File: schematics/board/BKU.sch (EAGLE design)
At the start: 83 parts, among them IC1 MAX809REUR, IC2 MAX809REUR, J1 idc_2x5, J2 idc_2x5, Q1 8MHz, Q2 32,768KHz, SW1 RST, SW2 RST, U1 STM32F405RGT6

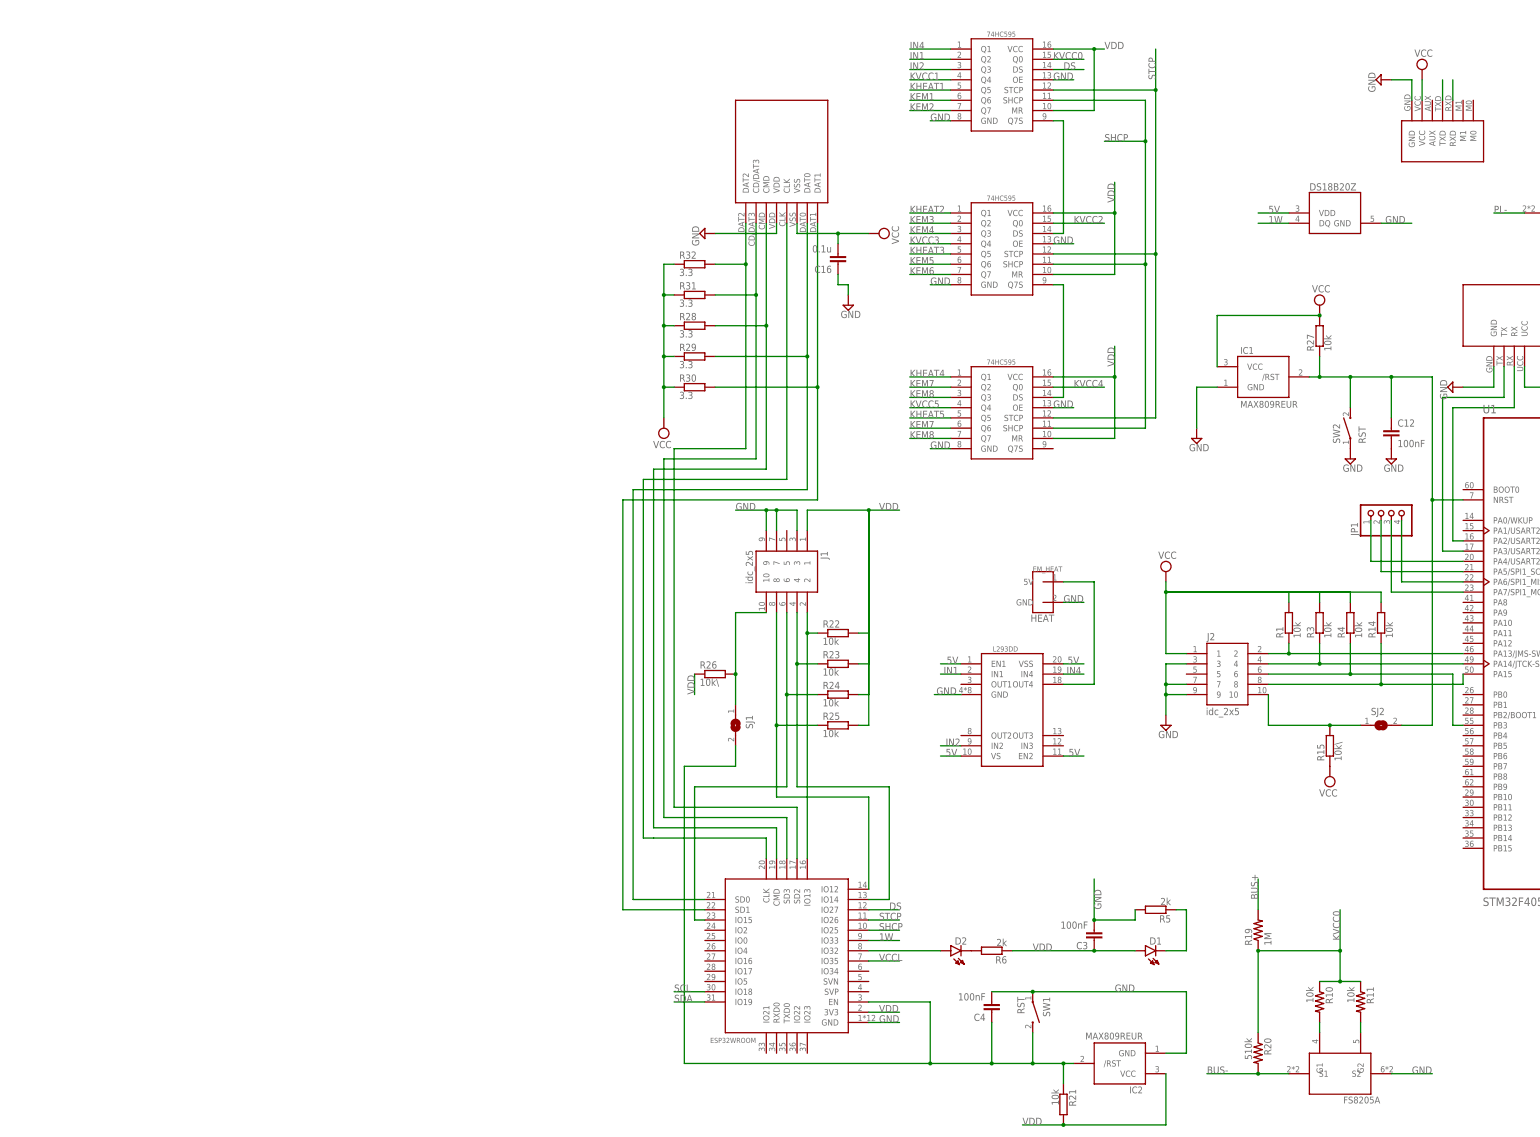
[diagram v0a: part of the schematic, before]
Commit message: доработана схема БСК1
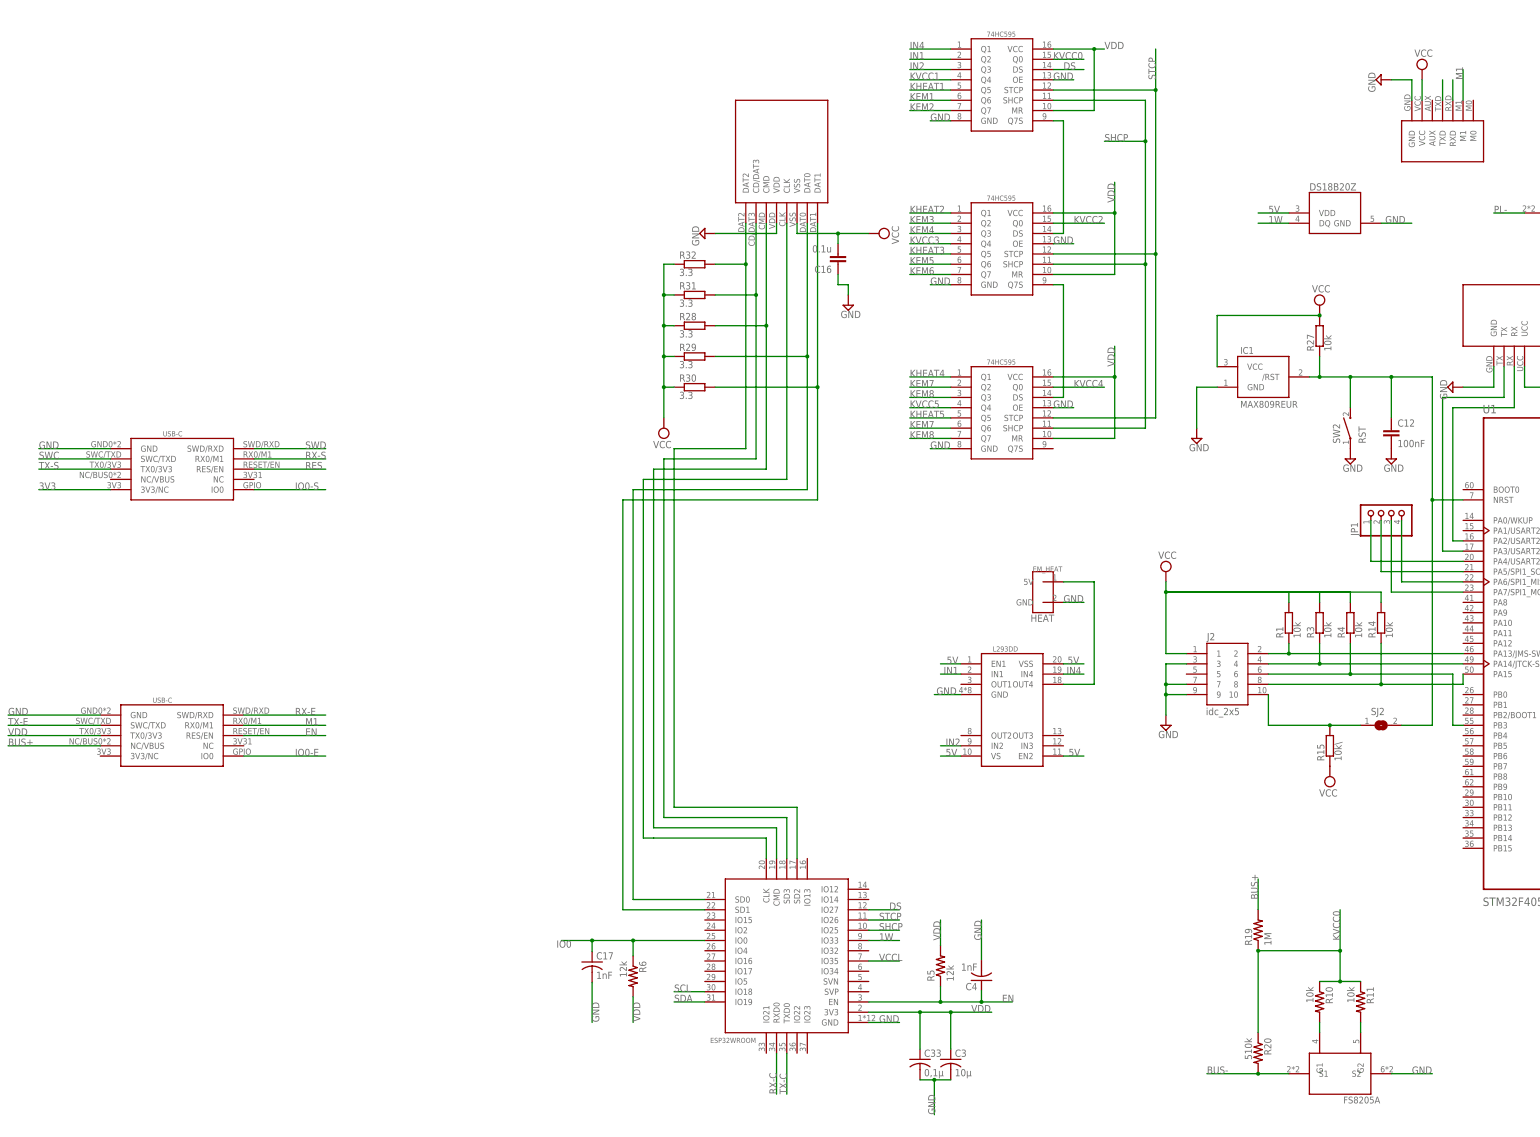
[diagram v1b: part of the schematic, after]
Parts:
- removed D1, D2: HLMP6, display-hp:HLMP6
- removed IC2: MAX809REUR, MAX809_:MAX809EUR
- removed J1: idc_2x5, idc_2x5:3221-10-0100-00
- removed R21, R22, R23, R24, R25: 10k, resistor-shunt:BVS
- removed R26: 10k\, resistor-shunt:BVS
- removed SJ1: (no value), jumper:SJW
- removed SW1: RST, 1437566-3:1437566-3
- added C17: 1nF, rcl:C-USC0603
- added C33: 0,1µ, rcl:C-USC0603
- added U$4, U$6: USB-C, CanCubeSat:USB-C
- C3: value 100nF -> 10µ; device rcl:C-EUC0603 -> rcl:C-USC0603
- C4: value 100nF -> 1nF; device rcl:C-EUC0603 -> rcl:C-USC0603
- R5, R6: value 2k -> 12k; device resistor-shunt:BVS -> resistor:R-US_R0603
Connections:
- removed net N$17: D1.K, R5.2
- removed net N$18: D2.K, R6.1
- removed net N$21: C4.1, IC2./RST, R21.2, SJ1.2, SW1.2, U$13.EN
- removed net N$22: J1.2, R22.2, U$13.IO13
- removed net N$23: J1.4, R23.2, U$13.IO14
- removed net N$26: J1.8, R25.2, U$13.IO12
- removed net N$27: J1.6, R24.2, U$13.IO15
- removed net N$29: J1.10, R26.1, SJ1.1
- removed net VDD3: D2.A, U$13.IO32
- new net 3V3: U$4.3V3/NC
- new net EN: C4.1, R5.1, U$13.EN, U$6.RES/EN
- new net IO0: C17.1, R6.1, U$13.IO0
- new net IO0-E: U$6.IO0
- new net IO0-S: U$4.IO0
- new net M1: U$2.M1, U$6.RX0/M1
- new net RES: U$4.RES/EN
- new net RX-C: U$13.RXD0
- new net RX-E: U$6.SWD/RXD
- new net RX-S: U$4.RX0/M1
- new net SWC: U$4.SWC/TXD
- new net SWD: U$4.SWD/RXD
- new net TX-C: U$13.TXD0
- new net TX-E: U$6.SWC/TXD
- new net TX-S: U$4.TX0/3V3
- net BUS+: now also U$6.NC/VBUS
- net GND: now also C17.2, C33.2, U$4.GND, U$6.GND; no longer IC2.GND, J1.3, J1.7, J1.9, R5.1, SW1.1
- net VDD: now also C33.1, R5.2, U$6.TX0/3V3; no longer D1.A, IC2.VCC, J1.1, R21.1, R22.1, R23.1, R24.1, R25.1, R26.2
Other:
- moved on the sheet: C3, C4

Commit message: доработаны схемы БСК1 и БКУ
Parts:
- removed C17: 1nF, rcl:C-USC0603
- removed R7: 10k, resistor:R-US_R0603
- removed U$14, U$16: FS8205A, CanCubeSat:FS8205A
- removed U$15, U$17: 74HC595, CanCubeSat:74HC595
- removed VAR1, VAR1A: (no value), pinheadCS:PINHD-1X8
- removed VAR2, VAR3: (no value), pinheadCS:PINHD-1X12
- added BSK2, BSK2A: (no value), pinheadCS:PINHD-1X8
- added BSK3: (no value), pinheadCS:PINHD-1X12
- added BSK4: (no value), pinheadCS:PINHD-1X14
- added LED1: (no value), led:LEDCHIPLED_0603
- added U$18, U$19, U$20: 74HC595, CanCubeSat:74HC595
- R2: value 10k -> 2k
- R6: value 12k -> 5k
- U$5: value DS18B20ZDS18B20Z -> DS18B20Z; device CanCubeSat:DS18B20ZDS18B20Z -> CanCubeSat:DS18B20Z
- U$9: value 74HC595 -> FS8205A+; device CanCubeSat:74HC595 -> CanCubeSat:FS8205A+
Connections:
- removed net IN1: U$8.IN1, U$9.Q2
- removed net IN2: U$8.IN2, U$9.Q3
- removed net IN4: U$8.IN4, U$9.Q1
- removed net IO0: C17.1, R6.1, U$13.IO0
- removed net KEM1: U$9.Q6, VAR1.3
- removed net KEM10: VAR3.4
- removed net KEM2: U$9.Q7, VAR1.2
- removed net KEM3: U$15.Q2, VAR1A.3
- removed net KEM4: U$15.Q3, VAR1A.2
- removed net KEM5: U$15.Q6, VAR2.5
- removed net KEM6: U$15.Q7, VAR2.4
- removed net KEM7: U$17.Q2, U$17.Q6, VAR2.2
- removed net KEM8: U$17.Q3, U$17.Q7, VAR2.1
- removed net KEM9: VAR3.5
- removed net KHEAT1: U$9.Q5, VAR1.4
- removed net KHEAT2: U$15.Q1, VAR1A.4
- removed net KHEAT3: U$15.Q5, VAR2.6
- removed net KHEAT4: U$17.Q1, VAR2.11
- removed net KHEAT5: U$17.Q5, VAR3.6
- removed net KVCC0: R10.1, R11.1, R19.1, R20.1, U$9.Q0
- removed net KVCC1: U$9.Q4, VAR1.5
- removed net KVCC2: U$15.Q0, VAR1A.5
- removed net KVCC3: U$15.Q4, VAR2.7
- removed net KVCC4: U$17.Q0, VAR2.12
- removed net KVCC5: U$17.Q4, VAR3.7
- removed net N$19: U$15.DS, U$9.Q7S
- removed net N$20: U$15.Q7S, U$17.DS
- removed net N$45: U$2.RXD
- removed net N$46: U$2.TXD
- removed net N$6: R28.2, R29.2, R30.2, R31.2, R32.2, R7.2, U$16.G2
- removed net PL-: U$16.S1, VAR3.1
- removed net RES: U$4.RES/EN
- removed net RX-C: U$13.RXD0
- removed net SCL: U$13.IO18, VAR3.11
- removed net SDA: U$13.IO19, VAR3.12
- removed net TX-C: U$13.TXD0
- removed net VCC: C16.2, C2.1, D3.A, D4.A, IC1.VCC, J2.1, R1.1, R14.1, R15.2, R27.1, R3.1, R4.1, U$1.UCC, U$2.VCC, U$3.VSS, U1.VDD
- removed net VCCL: R2.1, R7.1, U$13.IO35
- new net B1_KEM+: U$18.Q2, U$8.IN1
- new net B1_KEM-: U$18.Q3, U$8.IN2
- new net B1_KHEAT: U$18.Q1, U$8.IN4
- new net B1_KVCC: R10.1, R11.1, R19.1, R20.1, U$18.Q0
- new net B2A_KEM+: BSK2A.3, U$19.Q2
- new net B2A_KEM-: BSK2A.2, U$19.Q3
- new net B2A_KHEAT: BSK2A.4, U$19.Q1
- new net B2A_KVCC: BSK2A.5, U$19.Q0
- new net B2_KEM+: BSK2.3, U$18.Q6
- new net B2_KEM-: BSK2.2, U$18.Q7
- new net B2_KHEAT: BSK2.4, U$18.Q5
- new net B2_KVCC: BSK2.5, U$18.Q4
- new net B3_KEM+: BSK3.5, U$20.Q6
- new net B3_KEM-: BSK3.4, U$20.Q7
- new net B3_KHEAT: BSK3.6, U$20.Q5
- new net B3_KVCC: BSK3.7, U$20.Q4
- new net B4_KEM+: BSK4.11, U$19.Q6
- new net B4_KEM-: BSK4.10, U$19.Q7
- new net B4_KHEAT: BSK4.12, U$19.Q5
- new net B4_KVCC: BSK4.13, U$19.Q4
- new net B5_KEM+: BSK3.2, U$20.Q2
- new net B5_KEM-: BSK3.1, U$20.Q3
- new net B5_KHEAT: BSK3.11, U$20.Q1
- new net B5_KVCC: BSK3.12, U$20.Q0
- new net I2CINT: BSK4.5, U$13.IO18
- new net IO1: R2.1, U$13.IO5
- new net N$17: U$18.Q7S, U$19.DS
- new net N$18: U$19.Q7S, U$20.DS
- new net NRST: U$4.NRST/EN
- new net PL_KVCC: BSK4.8, U$13.IO33
- new net RX-R: U$13.IO35, U$2.TXD, U$6.RX0
- new net SCLTM: BSK4.7, U$13.IO16
- new net SDATM: BSK4.6, U$13.IO17
- new net TIME: BSK4.4, U$13.IO19
- new net TX-R: U$13.IO32, U$2.RXD, U$6.TX0
- net 1W: now also BSK2.6, BSK2A.6, BSK3.8, BSK4.14, U$13.IO21; no longer U$13.IO33, VAR1.6, VAR1A.6, VAR2.8, VAR3.8
- net 3V3: now also U$4.3V3/BUS; no longer U$4.3V3/NC
- net 5V: now also BSK2.7, BSK2A.7, BSK3.9, BSK4.2; no longer VAR1.7, VAR1A.7, VAR2.9, VAR3.9
- net BUS+: now also BSK2.8, BSK2A.8, BSK3.10, BSK4.3, U$6.3V3/BUS; no longer U$6.NC/VBUS, VAR1.8, VAR1A.8, VAR2.10, VAR3.10
- net BUS-: now also U$9.S1; no longer U$14.S1
- net DS: now also U$18.DS; no longer U$9.DS
- net EN: now also U$6.NRST/EN; no longer U$6.RES/EN
- net GND: now also BSK2.1, BSK2A.1, BSK3.3, BSK4.9, U$10.HEAT, U$13.HEAT, U$18.GND, U$18.OE, U$19.GND, U$19.OE, U$20.GND, U$20.OE, U$5.HEAT, U$8.HEAT, U$9.HEAT, U$9.S2; no longer C17.2, U$14.S2, U$15.GND, U$15.OE, U$16.S2, U$17.GND, U$17.OE, U$9.GND, U$9.OE, VAR1.1, VAR1A.1, VAR2.3, VAR3.3
- net IO0-E: now also R6.1, U$13.IO0, U$6.NC/GPIO; no longer U$6.IO0
- net IO0-S: now also U$4.NC/GPIO; no longer U$4.IO0
- net M1: now also U$13.IO34, U$6.NC/M1; no longer U$6.RX0/M1
- net N$4: now also LED1.C; no longer U$16.G1
- net N$8: now also U$9.G1; no longer U$14.G1
- net N$9: now also U$9.G2; no longer U$14.G2
- net RX-E: now also U$13.RXD0
- net RX-S: now also U$4.RX0; no longer U$4.RX0/M1
- net SHCP: now also U$18.SHCP, U$19.SHCP, U$20.SHCP; no longer U$15.SHCP, U$17.SHCP, U$9.SHCP
- net STCP: now also U$18.STCP, U$19.STCP, U$20.STCP; no longer U$15.STCP, U$17.STCP, U$9.STCP
- net TX-E: now also U$13.TXD0
- net TX-S: now also U$4.TX0; no longer U$4.TX0/3V3
- net VDD: now also BSK4.1, C16.2, C2.1, D3.A, D4.A, IC1.VCC, J2.1, LED1.A, R1.1, R14.1, R15.2, R27.1, R28.2, R29.2, R3.1, R30.2, R31.2, R32.2, R4.1, U$1.UCC, U$18.MR, U$18.VCC, U$19.MR, U$19.VCC, U$2.VCC, U$20.MR, U$20.VCC, U$3.VSS, U$6.NC/3V3, U1.VDD; no longer U$15.MR, U$15.VCC, U$17.MR, U$17.VCC, U$6.TX0/3V3, U$9.MR, U$9.VCC, VAR3.2
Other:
- moved on the sheet: R2, R6

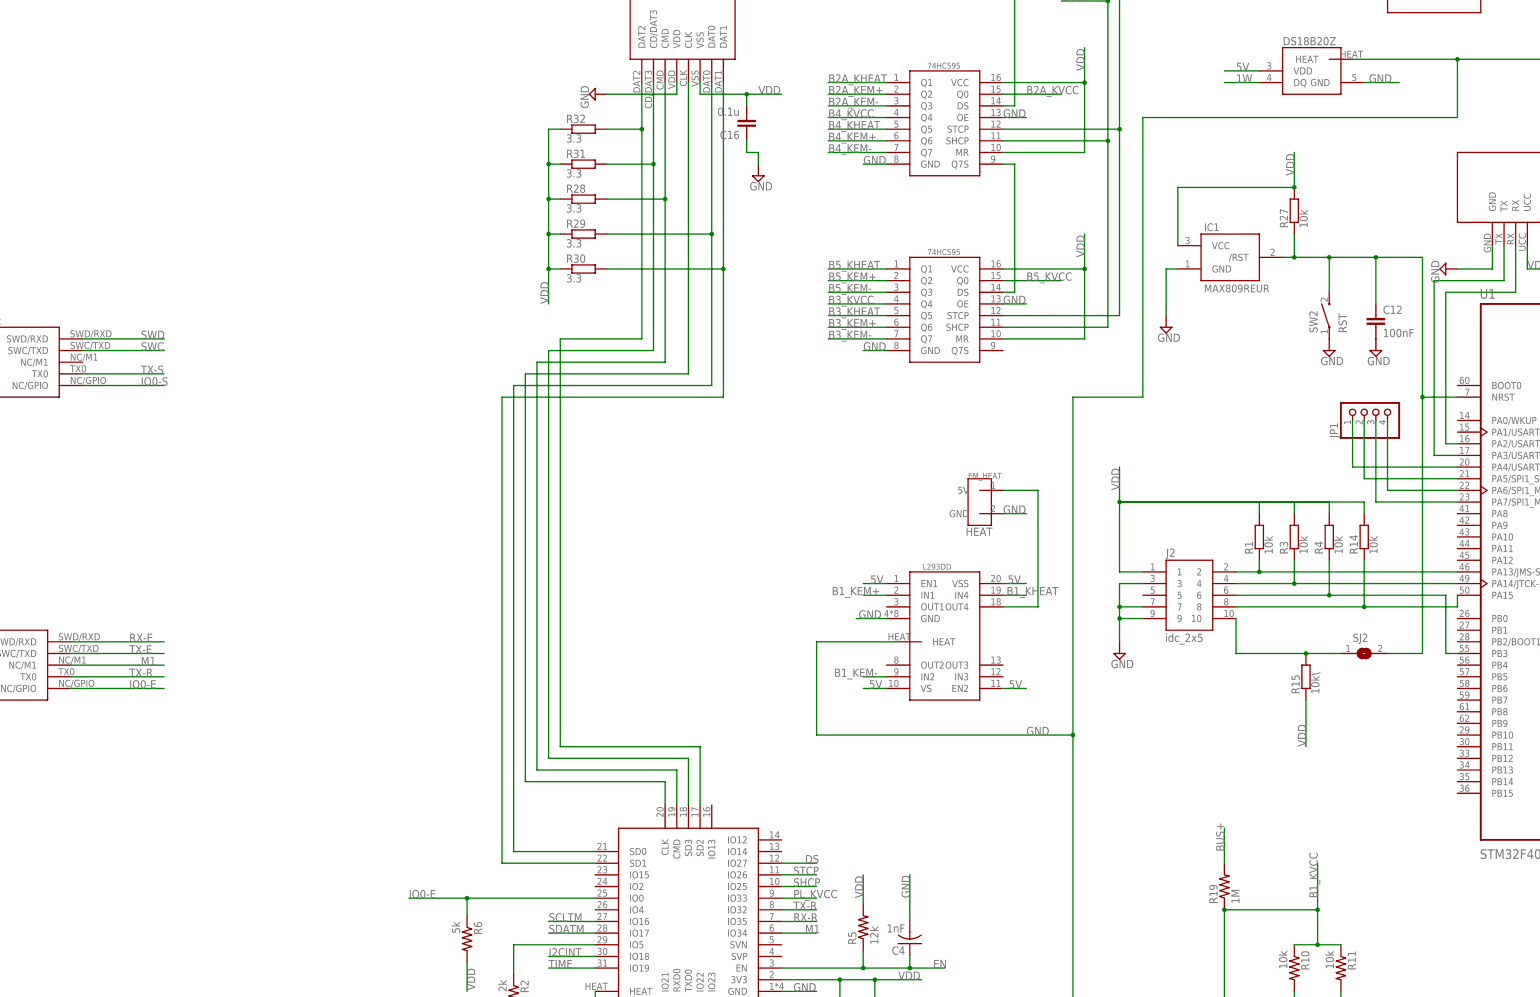
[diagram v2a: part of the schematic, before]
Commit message: обновлена схема БКУ
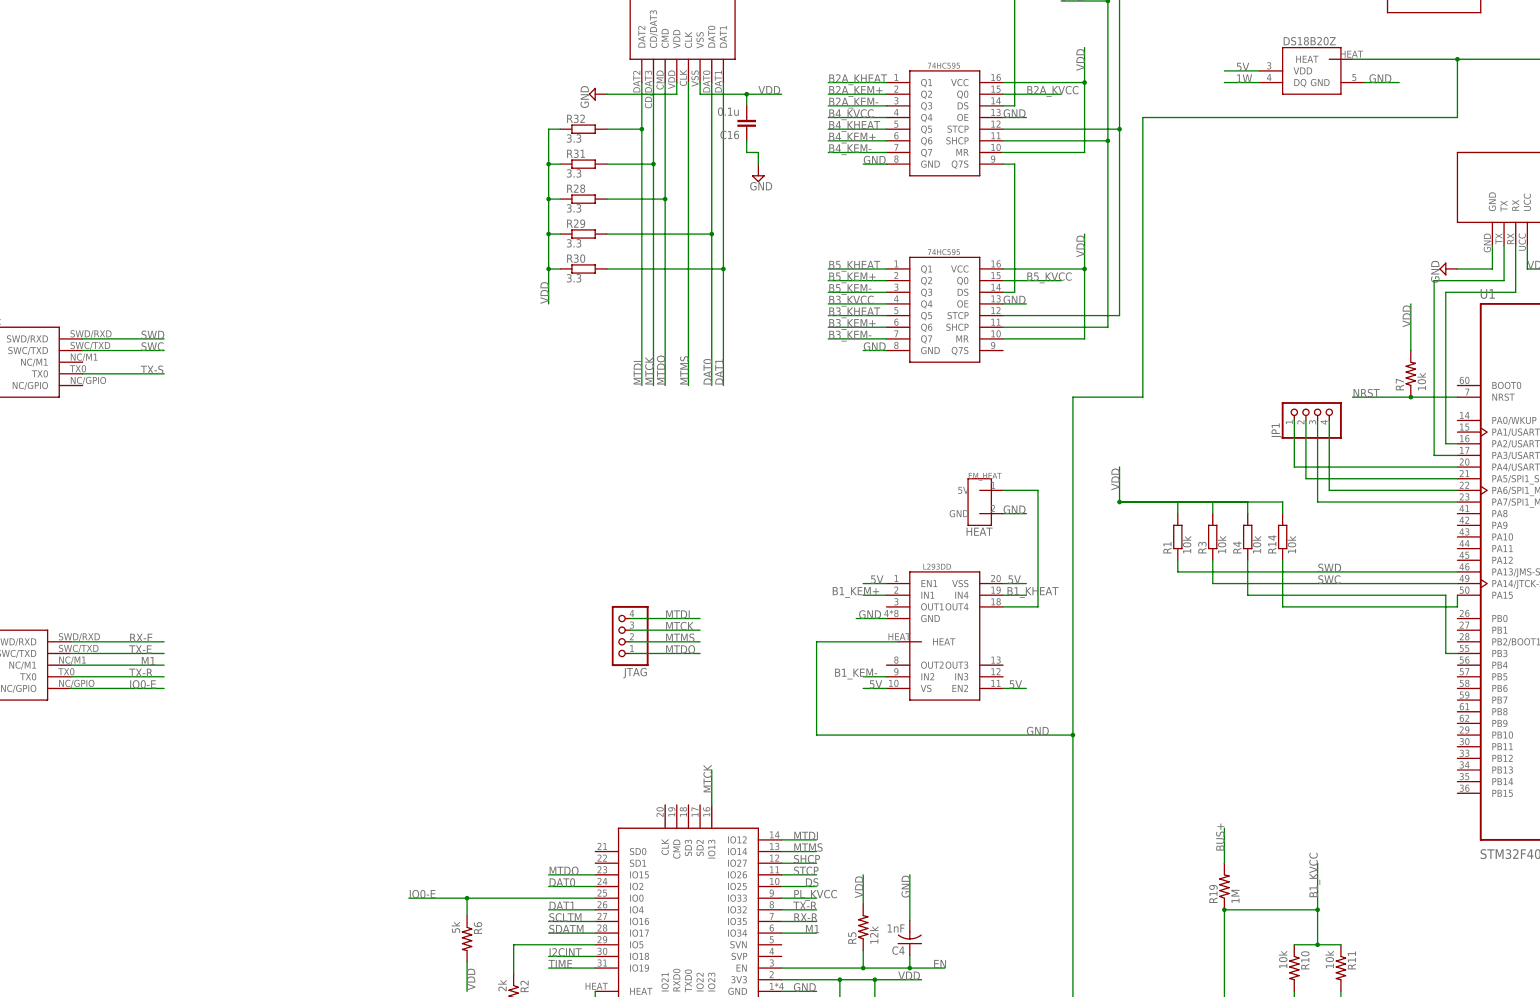
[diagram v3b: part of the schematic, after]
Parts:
- removed C12: 100nF, rcl:C-EUC0603
- removed IC1: MAX809REUR, MAX809_:MAX809EUR
- removed J2: idc_2x5, idc_2x5:3221-10-0100-00
- removed R15: 10k\, resistor-shunt:BVS
- removed R27: 10k, resistor-shunt:BVS
- removed SJ2: (no value), jumper:SJW
- removed SW2: RST, 1437566-3:1437566-3
- added JTAG: (no value), pinheadCS:PINHD-1X4
- added R7: 10k, resistor:R-US_R0603
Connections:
- removed net IO0-S: U$4.NC/GPIO
- removed net N$13: J2.10, R15.1, SJ2.1
- removed net N$14: C12.1, IC1./RST, R27.2, SJ2.2, SW2.2, U1.NRST
- removed net N$47: U$13.CLK, U$3.CLK
- removed net N$5: J2.2, R1.2, U1.PA13/JMS-SWDIO
- removed net N$51: R32.1, U$13.SD2, U$3.DAT2
- removed net N$52: R31.1, U$13.SD3, U$3.CD/DAT3
- removed net N$53: R28.1, U$13.CMD, U$3.CMD
- removed net N$55: R29.1, U$13.SD0, U$3.DAT0
- removed net N$56: R30.1, U$13.SD1, U$3.DAT1
- removed net N$7: J2.4, R3.2, U1.PA14/JTCK-SWCLK
- new net DAT0: R29.1, U$13.IO2, U$3.DAT0
- new net DAT1: R30.1, U$13.IO4, U$3.DAT1
- new net MTCK: JTAG.3, R31.1, U$13.IO13, U$3.CD/DAT3
- new net MTDI: JTAG.4, R32.1, U$13.IO12, U$3.DAT2
- new net MTDO: JTAG.1, R28.1, U$13.IO15, U$3.CMD
- new net MTMS: JTAG.2, U$13.IO14, U$3.CLK
- net DS: now also U$13.IO25; no longer U$13.IO27
- net GND: no longer C12.2, IC1.GND, J2.3, J2.7, J2.9, SW2.1
- net N$11: no longer J2.8
- net N$12: no longer J2.6
- net NRST: now also R7.1, U1.NRST
- net SHCP: now also U$13.IO27; no longer U$13.IO25
- net SWC: now also R3.2, U1.PA14/JTCK-SWCLK
- net SWD: now also R1.2, U1.PA13/JMS-SWDIO
- net VDD: now also R7.2; no longer IC1.VCC, J2.1, R15.2, R27.1
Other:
- moved on the sheet: JP1, R1, R14, R3, R4
